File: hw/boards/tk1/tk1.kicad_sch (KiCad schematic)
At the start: 2 parts

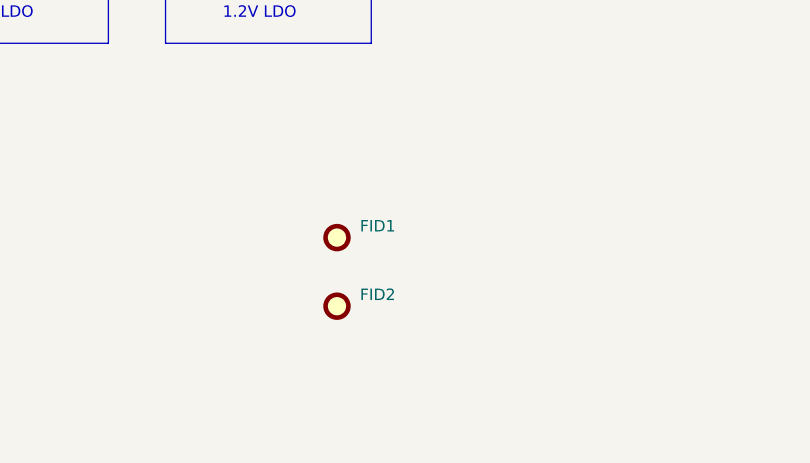
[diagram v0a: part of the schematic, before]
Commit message: Replaced Cap w. spring contacts
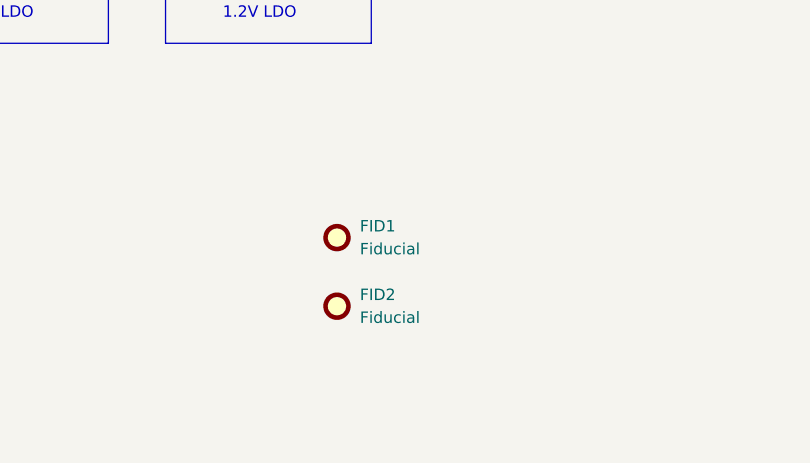
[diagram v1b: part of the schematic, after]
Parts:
- FID1, FID2: value (none) -> Fiducial; footprint (none) -> Fiducial:Fiducial_0.75mm_Mask1.5mm
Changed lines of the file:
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@@
       (effects (font (size 1.27 1.27)) (justify right))
     )
-    (property "Value" "" (id 1) (at 127 165.0999 90)
+    (property "Value" "Fiducial" (id 1) (at 127 165.0999 90)
       (effects (font (size 1.27 1.27)) (justify right))
     )
-    (property "Footprint" "" (id 2) (at 124.46 163.83 0)
+    (property "Footprint" "Fiducial:Fiducial_0.75mm_Mask1.5mm" (id 2) (at 124.46 163.83 0)
       (effects (font (size 1.27 1.27)) hide)
     )
@@
       (effects (font (size 1.27 1.27)) (justify right))
     )
-    (property "Value" "" (id 1) (at 127 172.7199 90)
+    (property "Value" "Fiducial" (id 1) (at 127 172.7199 90)
       (effects (font (size 1.27 1.27)) (justify right))
     )
-    (property "Footprint" "" (id 2) (at 124.46 171.45 0)
+    (property "Footprint" "Fiducial:Fiducial_0.75mm_Mask1.5mm" (id 2) (at 124.46 171.45 0)
       (effects (font (size 1.27 1.27)) hide)
     )
@@
       (reference "U10") (unit 1) (value "PT2043AT6") (footprint "Package_TO_SOT_SMD:SOT-23-6")
     )
-  )
+    (path "/00000000-0000-0000-0000-0000611cc101/81172fbc-f24e-4173-965f-d88ed2c48035"
+      (reference "U11") (unit 1) (value "~") (footprint "")
+    )
+  )
